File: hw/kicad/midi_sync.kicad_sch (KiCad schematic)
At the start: 18 parts, among them J301 MIDI IN TRS, U301 H11L1, U302 74LVC1G17

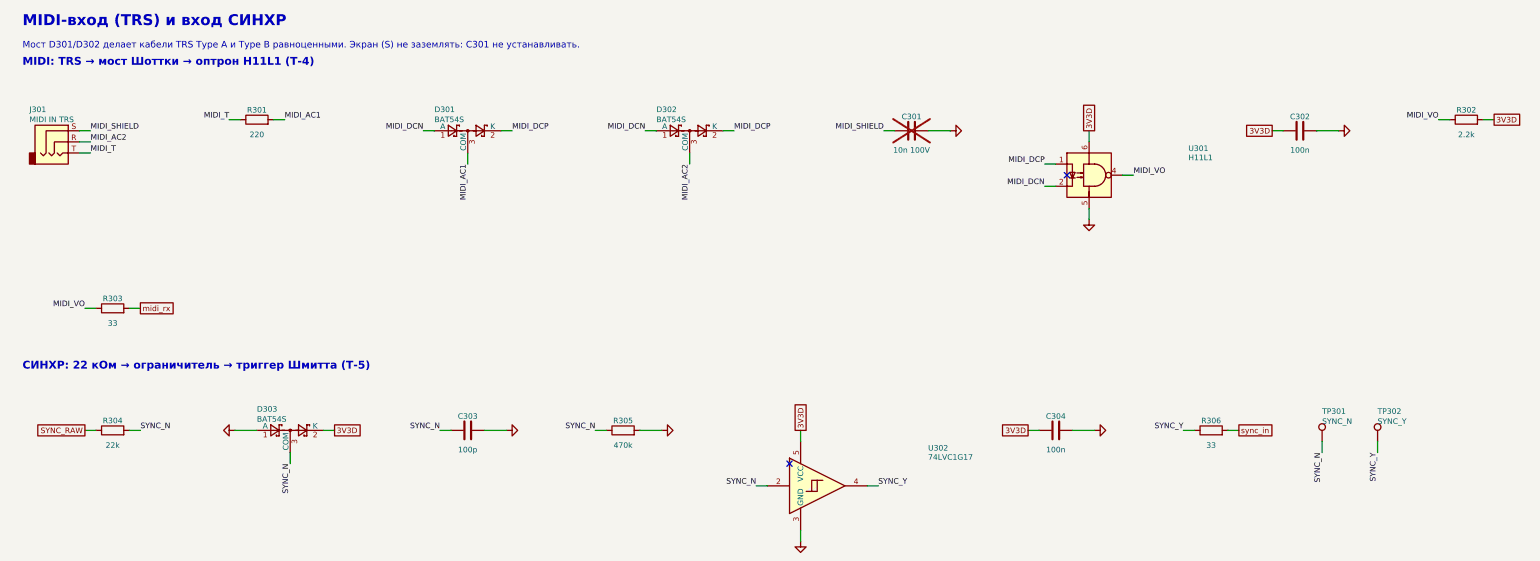
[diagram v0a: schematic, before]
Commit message: Reorganize KiCad schematic into 7 functional sheets with framed blocks
- Sheets: power, fpga, midi_sync, analog_in (inputs + ADC), audio_out
  (DAC + OUT/OUT2 + clip LEDs), phones, panel
- Each functional block is drawn in a dashed frame with a title; blocks are
  tiled across the sheet, A3/A2 chosen automatically
- Netlist check still 153/153; PDF and docs updated

Co-Authored-By: Claude Opus 5.5 <noreply@anthropic.com>
Claude-Session: https://claude.ai/code/session_01JcNV2ZCXWxtNzRVWffkrjk
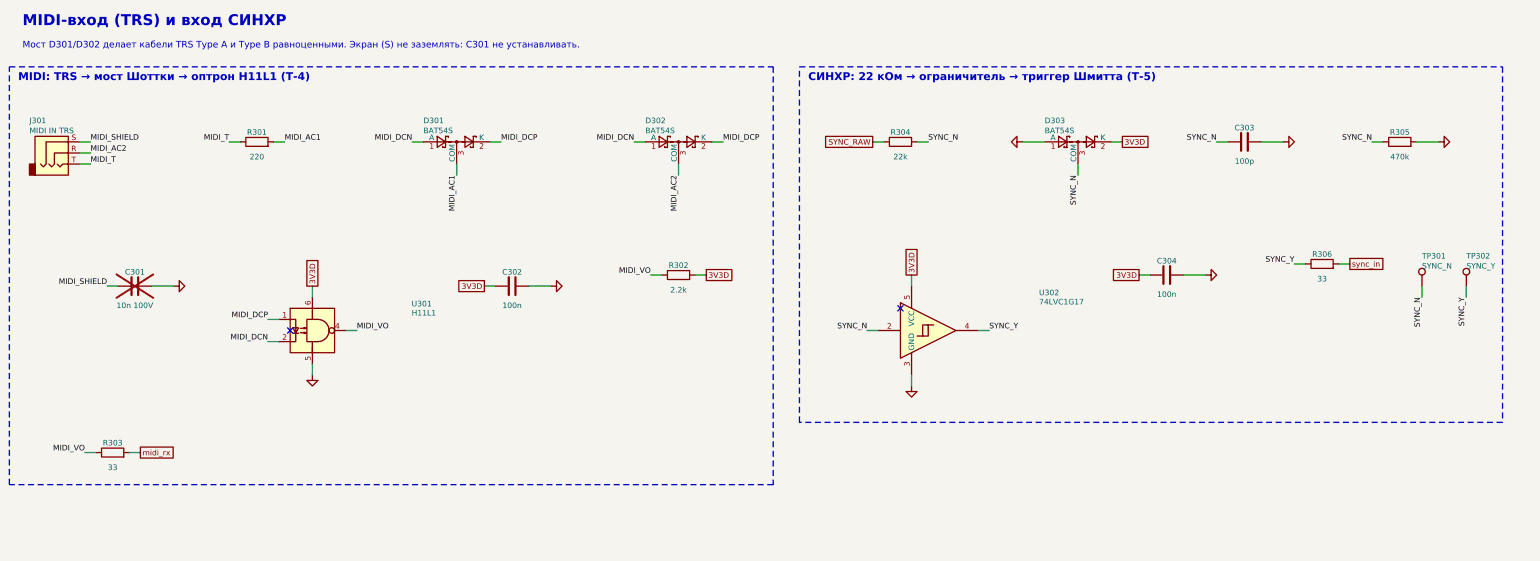
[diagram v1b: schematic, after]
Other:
- moved on the sheet: C301, C302, C303, C304, D301, D302, D303, J301, R301, R302, R303, R304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
